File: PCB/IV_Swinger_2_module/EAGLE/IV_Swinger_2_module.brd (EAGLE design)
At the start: 59.7 x 53.3 mm, 24 parts, among them J1 

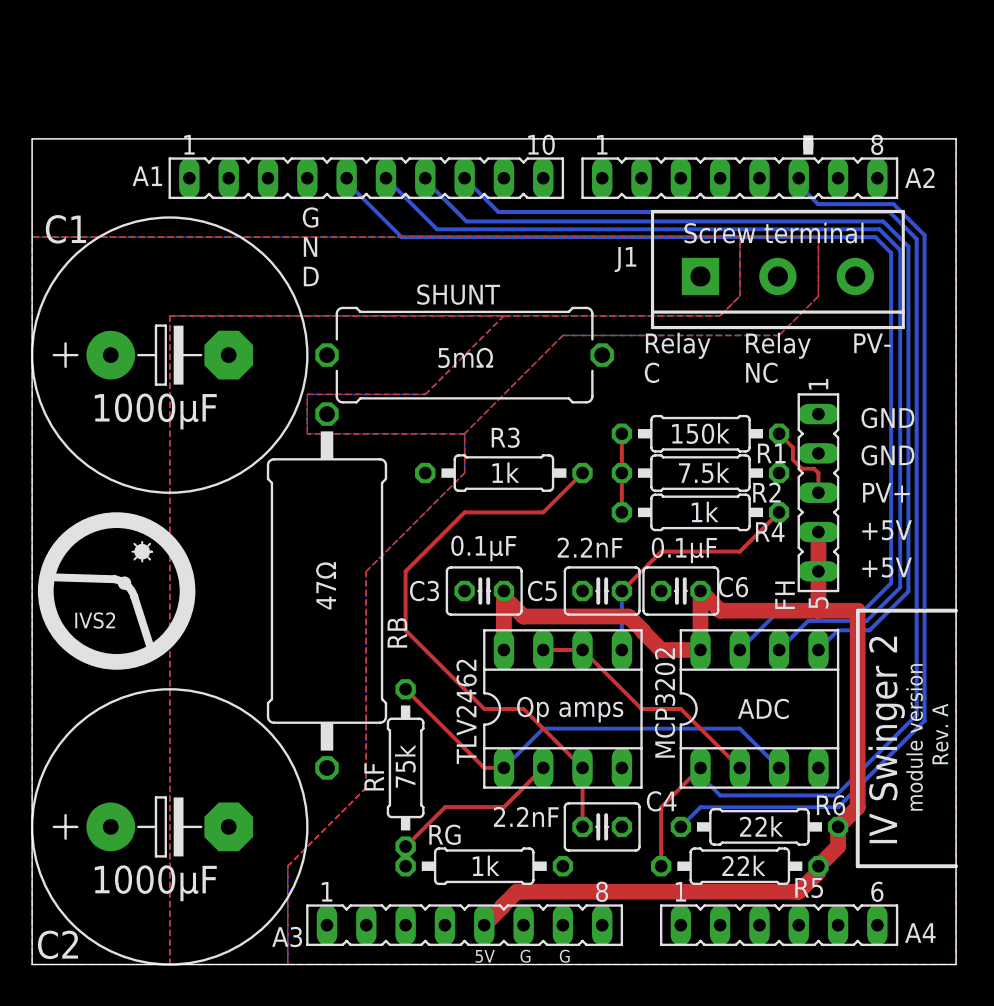
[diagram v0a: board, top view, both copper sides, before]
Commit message: Standard (EMR-based) PCB update to RevB
This is RevB of the standard IVS2 EMR-based module version PCB.  It is based on RevB of the SSR-based module version. The main purpose of this revision is to make the SSR and EMR versions as similar as possible, namely:

  - the connections to the binding posts are both on a screw-terminal block on the left end of the board (like SSR version)

  - pads are provided for the bypass diodes (like SSR version)

  - the current-carrying path from the shunt is now isolated in a stub off the ground plane (like SSR version)

  - R3 is now connected to the shunt with a dedicated trace (like SSR version)

  - Connections to EMR are from a second screw-terminal block that is located on the board where the SSRs are in the SSR version

Note that there is nothing "wrong", per se, with the RevA board. This just cleans a few things up and makes it much easier to compare it with the SSR version.
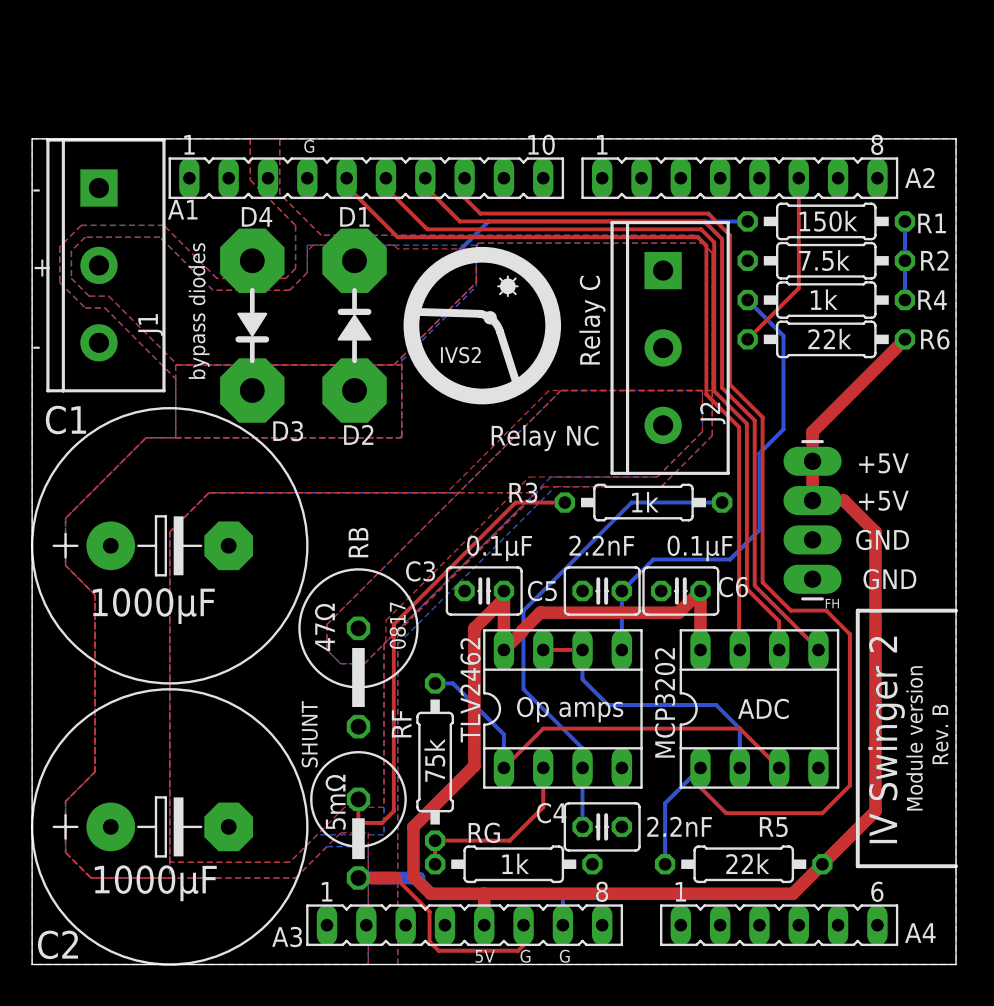
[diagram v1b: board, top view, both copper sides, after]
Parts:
- added D1, D2, D3, D4: WIREPAD4,16O1,6, wirepad:4,16O1,6
- added J2: (no value), SparkFun-Connectors:SCREWTERMINAL-5MM-3
- FH: device con-lsta:FE05-1 -> my_connectors:1X04_LONGPADS
- RB: device rcl:P0817/22 -> rcl:P0817V
- SHUNT: device rcl:0617/17 -> rcl:0617V
- moved J1 39.3 mm to (4.32, 50.2), turned to 270 degrees
- moved SHUNT 32.0 mm to (21.1, 8.13), turned to 270 degrees
- moved R6 31.8 mm to (51.3, 40.4), turned to 180 degrees
- moved R1 15.9 mm to (51.3, 48.0), turned to 180 degrees
- moved R2 15.9 mm to (51.3, 45.5), turned to 0 degrees
- moved R4 15.9 mm to (51.3, 42.9), turned to 180 degrees
- moved C1 12.3 mm to (8.89, 27.1)
- moved R3 9.22 mm to (39.5, 29.8)
- moved RB 7.76 mm to (21.1, 16.6), turned to 270 degrees
- moved FH 5.60 mm to (50.4, 24.9), turned to 90 degrees
- moved RF 1.94 mm to (26.0, 13.1)
- moved RG 1.91 mm to (31.1, 6.48)
- moved R5 0.28 mm to (46.0, 6.48)
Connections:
- net N10 renamed N14
- net N9 renamed N13
- removed net N2: R1.1, R2.2, R4.1
- removed net N3: A2.6, R6.1
- removed net N8: A1.5, MCP3202.7
- removed net RELAY_NC: J1.2, RB.2
- new net BLEED+: J2.3, RB.1
- new net N15: D2.1, D3.1
- new net N16: C4.1, R3.1, TLV2462.3
- new net N17: RF.2, RG.2, TLV2462.2
- new net PV+: D1.1, J1.2, R1.2
- net +5V: now also FH.3, R6.1; no longer FH.5, R6.2
- net GND: now also D4.1, J1.1, SHUNT.2; no longer SHUNT.1
- net LOAD_CAP+: now also J2.1, J2.2; no longer J1.1
- net LOAD_CAP-: now also RB.2, SHUNT.1; no longer RB.1, SHUNT.2
- net N1: now also A2.6, R6.2; no longer FH.3, R1.2
- net N11: now also R1.1, R2.2, R4.1; no longer C4.1, R3.1, TLV2462.3
- net N12: now also C5.1, R4.2, TLV2462.5; no longer RF.2, RG.2, TLV2462.2
- net N4: now also A1.8, MCP3202.1, R5.1; no longer C5.1, R4.2, TLV2462.5
- net N5: now also A1.7, MCP3202.5; no longer A1.8, MCP3202.1, R5.1
- net N6: now also A1.6, MCP3202.6; no longer A1.7, MCP3202.5
- net N7: now also A1.5, MCP3202.7; no longer A1.6, MCP3202.6
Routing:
- net N8: track 70.2 -> 0.00 mm
- net N4: track 16.1 -> 79.0 mm
- net N3: track 59.9 -> 0.00 mm
- net N5: track 86.1 -> 50.3 mm
- net +5V: track 78.9 -> 113.2 mm
- net N11: track 36.8 -> 5.08 mm
- net N16: track 0.00 -> 31.3 mm
- net GND: track 0.00 -> 30.9 mm
- net LOAD_CAP-: track 0.00 -> 30.5 mm
- net PV+: track 0.00 -> 19.6 mm
- net N12: track 12.3 -> 30.8 mm
- net N7: track 66.4 -> 52.4 mm
- net N17: track 0.00 -> 11.9 mm
- net N6: track 62.8 -> 51.4 mm
- net N1: track 5.33 -> 11.8 mm
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- added copper zone on layer 1, net BLEED+
- added copper zone on layer 16, net BLEED+
- added copper zone on layer 1, net N15
- added copper zone on layer 16, net N15
- added copper zone on layer 1, net PV+
- added copper zone on layer 16, net PV+
- removed copper zone on layer 1, net RELAY_NC
- removed copper zone on layer 16, net RELAY_NC
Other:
- board text added: "+"
- board text added: "-"
- board text added: "150k"
- board text added: "1k"
- board text added: "22k"
- board text added: "7.5k"
- board text added: "75k"
- board text added: "Module version"
- board text added: "Rev. B"
- board text added: "bypass diodes"
- board text removed: "."
- board text removed: "G N D"
- board text removed: "PV+"
- board text removed: "PV-"
- board text removed: "Rev. A"
- board text removed: "Screw terminal"
- board text removed: "module version"
